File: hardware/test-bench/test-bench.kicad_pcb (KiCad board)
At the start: 2 copper layers, 90 x 90 mm, 37 parts, among them J1 Conn_Mem_Ext, J2 Conn_Reg, J3 SWD, J4 Conn_Mem, J5 FTDI, J6 Conn_Power, SW1 SW_Push_4pin, SW2 SW_Push_4pin, U1 STM32G030F6, U2 MCP23S17_SS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

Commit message: Added ~RESET to memory bus
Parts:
- removed R1, R2: DNP, Resistor_SMD:R_0805_2012Metric
- removed R3, R4: 0, Resistor_SMD:R_0805_2012Metric
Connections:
- J1 pad 28: Net-(J1-Pad28) -> /~RESET
- U1 pad 10: /UART2_RX -> /FTDI_TX
- U1 pad 9: /UART2_TX -> /FTDI_RX
- U4 pad 3: Net-(J1-Pad28) -> Net-(J1-Pad27)
- U4 pad 4: Net-(J1-Pad27) -> Net-(J1-Pad26)
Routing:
- net /~RESET: track 123.7 -> 164.2 mm, vias 8 -> 10
- net /UART2_RX: track 30.6 -> 0.00 mm
- net /UART2_TX: track 28.2 -> 0.00 mm
- net /FTDI_RX: track 12.4 -> 39.8 mm
- net /FTDI_TX: track 12.3 -> 38.6 mm
- net Net-(J1-Pad26): track 0.00 -> 17.2 mm
- net Net-(J1-Pad28): track 16.1 -> 0.00 mm
- net Net-(J1-Pad27): track 14.0 -> 13.0 mm

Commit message: Unified footprints
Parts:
- C1, C2, C3, C4, C5, C6, C7, C8: footprint Capacitor_SMD:C_0805_2012Metric -> Capacitor_SMD:C_0805_2012Metric_Pad1.15x1.40mm_HandSolder
- R5, R6, R7, R8: footprint Resistor_SMD:R_0805_2012Metric -> Resistor_SMD:R_0805_2012Metric_Pad1.15x1.40mm_HandSolder
- U6: footprint Package_TO_SOT_SMD:SOT-23-5 -> Package_TO_SOT_SMD:SOT-23-5_HandSoldering
- moved R6 0.13 mm to (178.7, 56.3)
- moved R5 0.08 mm to (170.7, 56.3)
- moved R8 0.06 mm to (175.0, 38.1)
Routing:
- net VCC: track 225.0 -> 225.6 mm, vias 9 -> 8

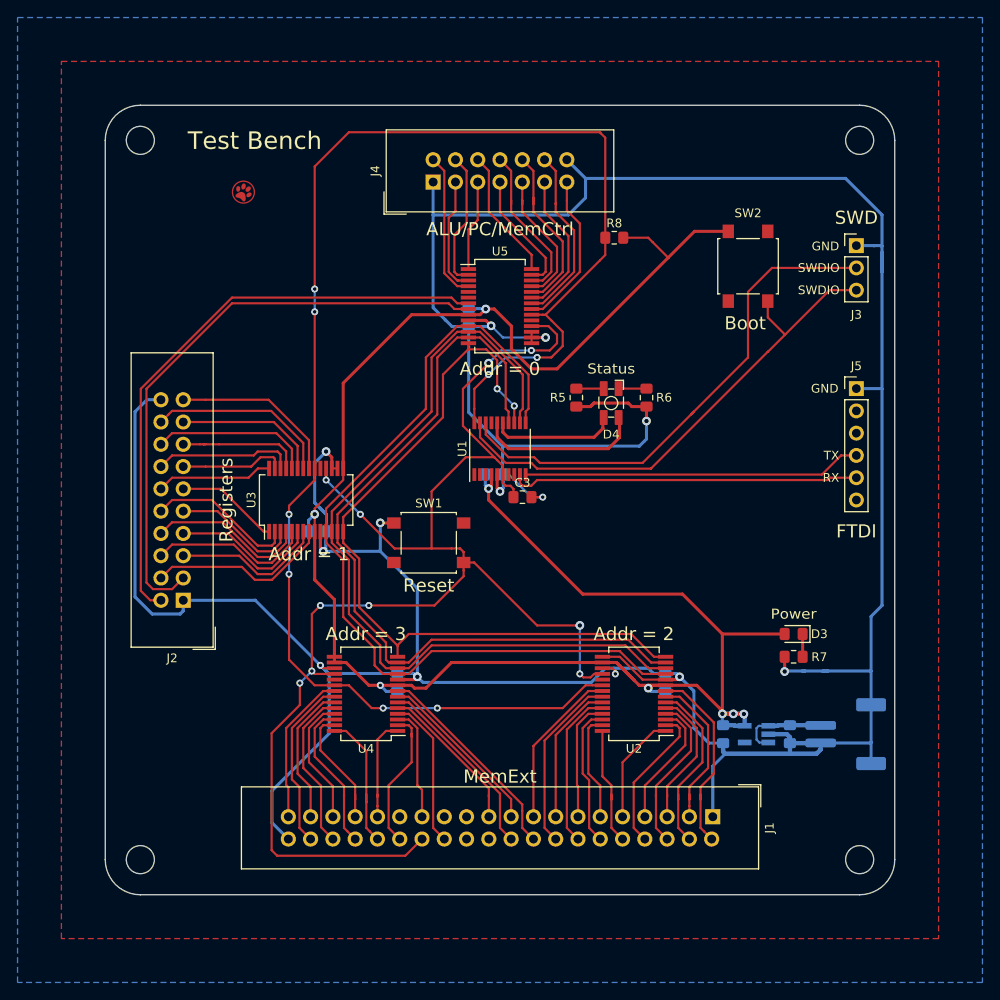
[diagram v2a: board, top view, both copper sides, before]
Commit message: Fully connect test headers
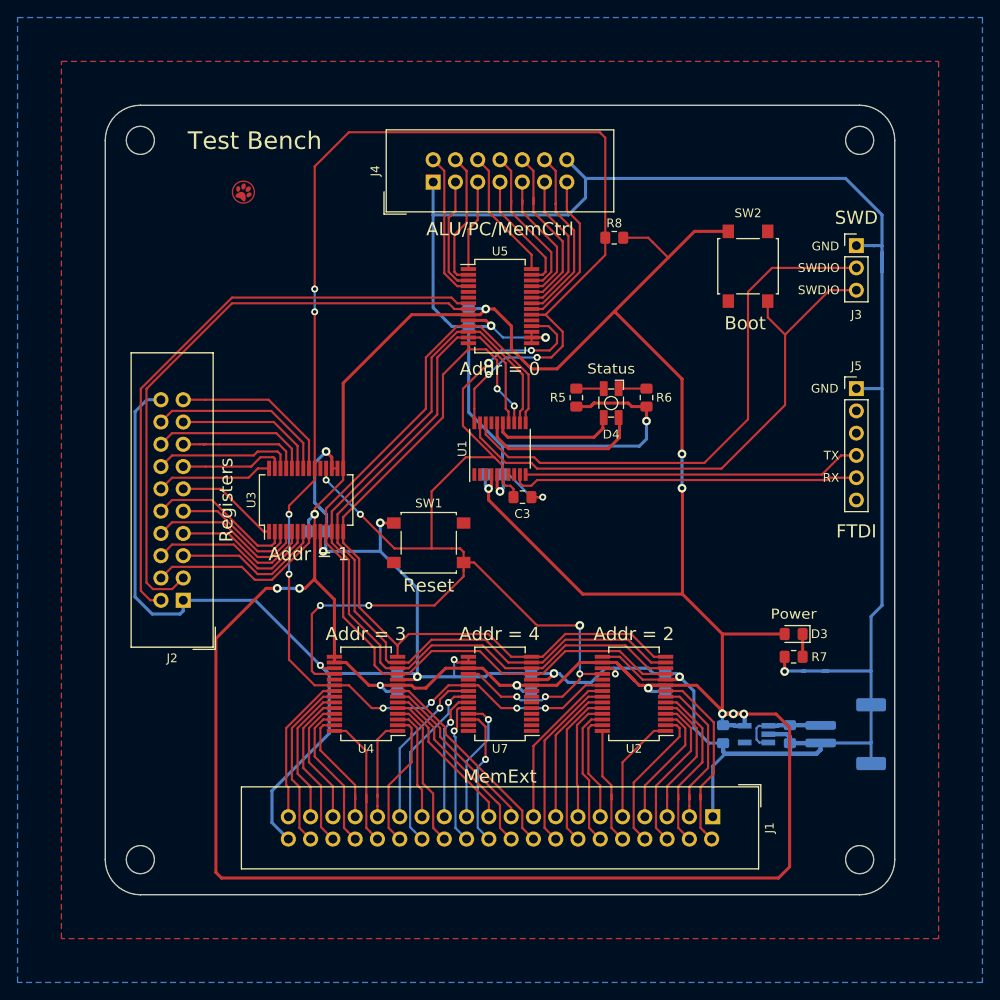
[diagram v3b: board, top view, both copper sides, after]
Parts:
- added C9: 100n, Capacitor_SMD:C_0805_2012Metric_Pad1.15x1.40mm_HandSolder, B.Cu at (165.6, 88.8)
- added U7: MCP23S17_SS, Package_SO:SSOP-28_5.3x10.2mm_P0.65mm, F.Cu at (162.0, 90.1)
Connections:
- net Net-(D3-Pad1) renamed /LED_POWER_K
- net Net-(D4-Pad3) renamed /LED_R_K
- net Net-(D4-Pad4) renamed /LED_G_K
- net Net-(J1-Pad10) renamed /IO2A7
- net Net-(J1-Pad11) renamed /IO2A6
- net Net-(J1-Pad12) renamed /IO2A5
- net Net-(J1-Pad13) renamed /IO2A4
- net Net-(J1-Pad14) renamed /IO2A3
- net Net-(J1-Pad15) renamed /IO2A2
- net Net-(J1-Pad16) renamed /IO2A1
- net Net-(J1-Pad17) renamed /IO2A0
- net Net-(J1-Pad18) renamed /IO3B7
- net Net-(J1-Pad19) renamed /IO3B6
- net Net-(J1-Pad2) renamed /IO2B7
- net Net-(J1-Pad20) renamed /IO3B5
- net Net-(J1-Pad21) renamed /IO3B4
- net Net-(J1-Pad26) renamed /IO3B3
- net Net-(J1-Pad27) renamed /IO3B2
- net Net-(J1-Pad3) renamed /IO2B6
- net Net-(J1-Pad30) renamed /IO3B1
- net Net-(J1-Pad31) renamed /IO3B0
- net Net-(J1-Pad32) renamed /IO3A7
- net Net-(J1-Pad33) renamed /IO3A6
- net Net-(J1-Pad34) renamed /IO3A5
- net Net-(J1-Pad35) renamed /IO3A4
- net Net-(J1-Pad36) renamed /IO3A3
- net Net-(J1-Pad37) renamed /IO3A2
- net Net-(J1-Pad38) renamed /IO3A1
- net Net-(J1-Pad39) renamed /IO3A0
- net Net-(J1-Pad4) renamed /IO2B5
- net Net-(J1-Pad5) renamed /IO2B4
- net Net-(J1-Pad6) renamed /IO2B3
- net Net-(J1-Pad7) renamed /IO2B2
- net Net-(J1-Pad8) renamed /IO2B1
- net Net-(J1-Pad9) renamed /IO2B0
- J1 pad 22: Net-(J1-Pad22) -> /IO4A5
- J1 pad 23: Net-(J1-Pad23) -> /IO4A4
- J1 pad 24: Net-(J1-Pad24) -> /IO4A3
- J1 pad 25: Net-(J1-Pad25) -> /IO4A2
- J1 pad 28: /~RESET -> /IO4A1
- J1 pad 29: Net-(J1-Pad29) -> /IO4A0
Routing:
- net VCC: track 225.6 -> 393.2 mm, vias 8 -> 13
- net /~RESET: track 164.1 -> 138.8 mm
- net /IO4A1: track 0.00 -> 21.3 mm, vias 0 -> 1
- net /IO4A0: track 0.00 -> 18.9 mm, vias 0 -> 1
- net /IO4A3: track 0.00 -> 16.8 mm, vias 0 -> 1
- net /IO4A5: track 0.00 -> 16.0 mm, vias 0 -> 1
- net /IO4A2: track 0.00 -> 14.8 mm, vias 0 -> 1
- net /IO4A4: track 0.00 -> 14.7 mm, vias 0 -> 1
- net GND: track 462.4 -> 469.9 mm, vias 13 -> 15
- net /SWCLK: track 59.1 -> 63.8 mm
- net /SWDIO: track 59.2 -> 62.8 mm
- net /MOSI: track 92.5 -> 94.7 mm
- net /~CS: track 98.9 -> 101.1 mm
- net /SCK: track 96.0 -> 98.1 mm
- net /MISO: track 88.2 -> 90.3 mm
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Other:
- board text added: "Addr = 4"

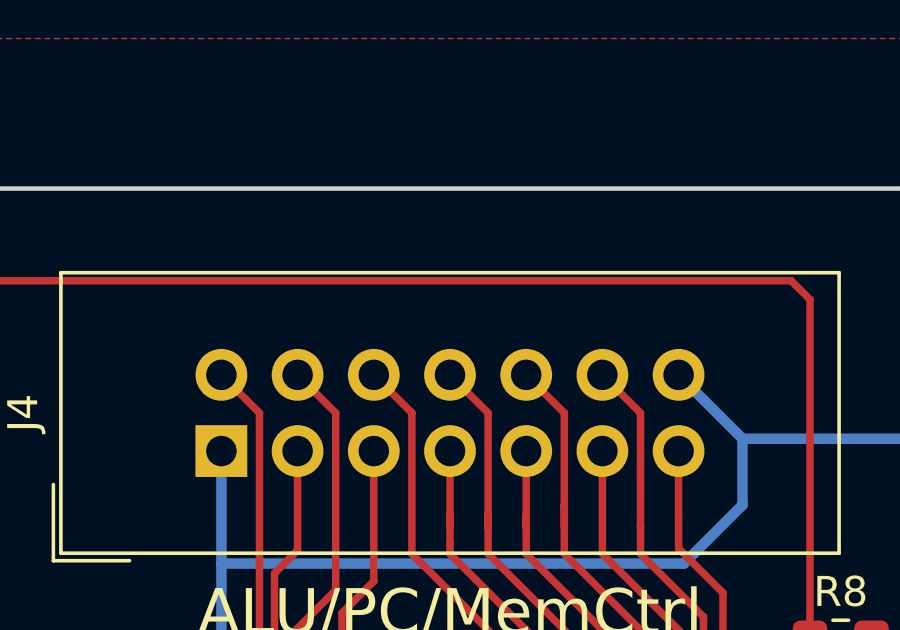
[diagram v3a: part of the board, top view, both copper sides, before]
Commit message: Added placeholders for JLCPCB serial numbers
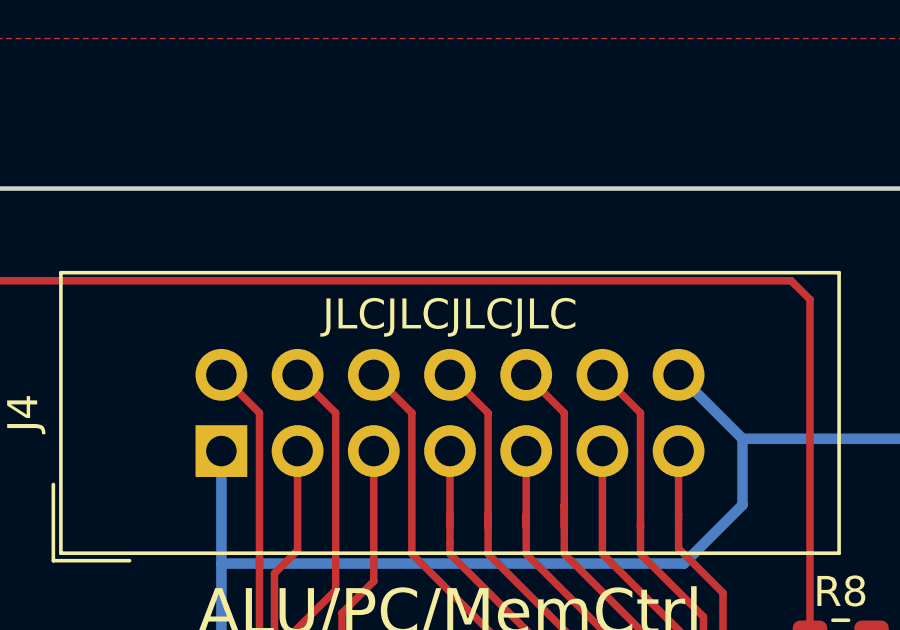
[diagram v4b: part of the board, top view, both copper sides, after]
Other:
- board text added: "JLCJLCJLCJLC"
